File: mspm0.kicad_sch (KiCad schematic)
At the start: 127 parts, among them J1 Barrel_Jack_Switch_Pin3Ring, J10 USB_C_Receptacle_PowerOnly_6P, J11 Conn_01x04_MountingPin, J12 Conn_01x18_Pin, J2 Conn_01x02_Pin, J3 Conn_01x04_Pin, J4 Conn_01x04_Pin, J5 Conn_01x04_MountingPin, J6 Conn_01x04_Pin, J7 Conn_01x04_Pin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

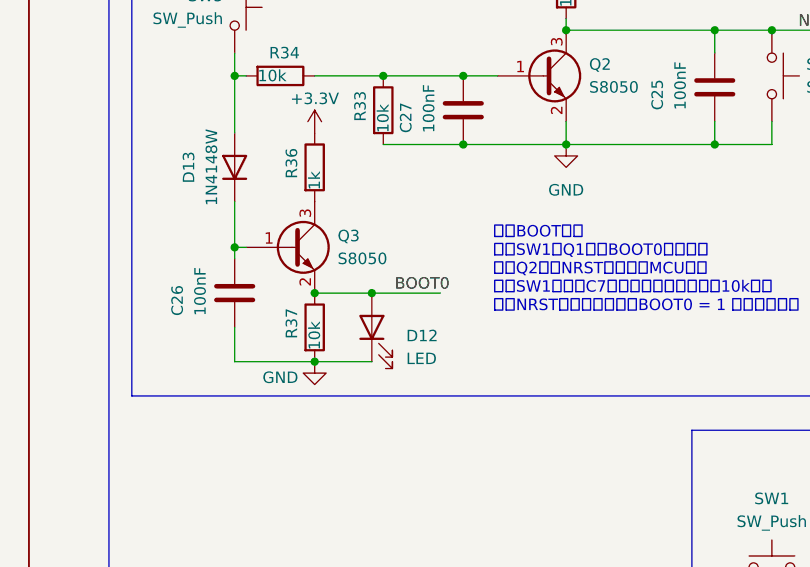
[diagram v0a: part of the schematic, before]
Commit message: fixed floating bsl_pin
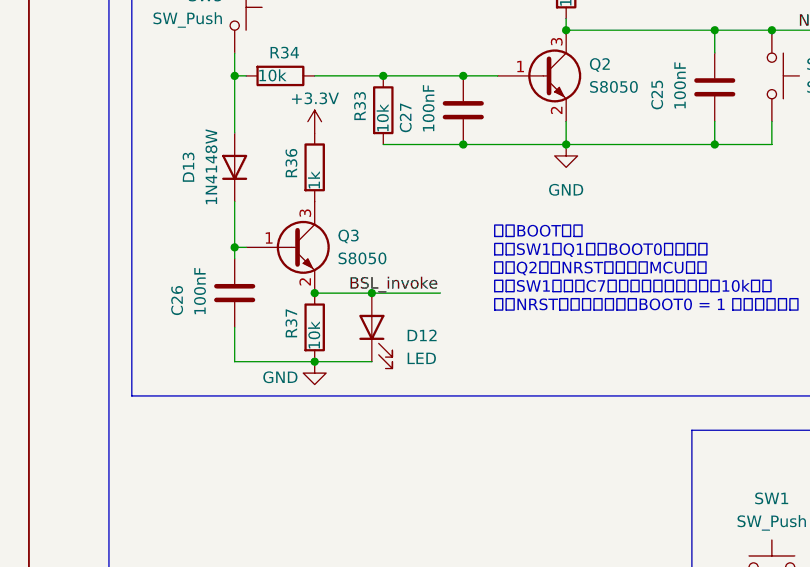
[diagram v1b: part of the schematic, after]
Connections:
- net BOOT0 is gone; now on net BSL_invoke: D12.2 (A), Q3.2 (E), R37.1
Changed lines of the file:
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@@
-		)
-	)
-	(label "BOOT0"
-		(at 153.67 90.17 0)
-		(fields_autoplaced yes)
-		(effects
-			(font
-				(size 1.27 1.27)
-			)
-			(justify left bottom)
 		)
 	)
@@
 			(font
 				(size 1.27 1.27)
+				(color 246 115 255 1)
 			)
 			(justify left bottom)
@@
 			(font
 				(size 1.27 1.27)
+				(color 0 255 11 1)
 			)
 			(justify left bottom)
@@
 			(font
 				(size 1.27 1.27)
+				(color 0 255 11 1)
 			)
 			(justify left bottom)
@@
 			(font
 				(size 1.27 1.27)
+				(color 246 115 255 1)
 			)
 			(justify left bottom)
@@
 			(font
 				(size 1.27 1.27)
+				(color 0 255 11 1)
 			)
 			(justify left bottom)
@@
 		)
 	)
+	(label "BSL_invoke"
+		(at 148.59 90.17 0)
+		(fields_autoplaced yes)
+		(effects
+			(font
+				(size 1.27 1.27)
+			)
+			(justify left bottom)
+		)
+	)
 	(label "PB20_A0_6"
 		(at 57.15 146.05 180)
@@
 			(font
 				(size 1.27 1.27)
+				(color 246 115 255 1)
 			)
 			(justify left bottom)
@@
 			(font
 				(size 1.27 1.27)
+				(color 0 255 11 1)
 			)
 			(justify left bottom)
@@
 			(font
 				(size 1.27 1.27)
-			)
-			(justify left bottom)
+				(color 246 115 255 1)
+			)
+			(justify left bottom)
